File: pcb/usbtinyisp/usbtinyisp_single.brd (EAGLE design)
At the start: 44 x 36 mm, 27 parts, among them IC1 ATTINY2313-20P, IC2 74LVX125D, Q1 12000

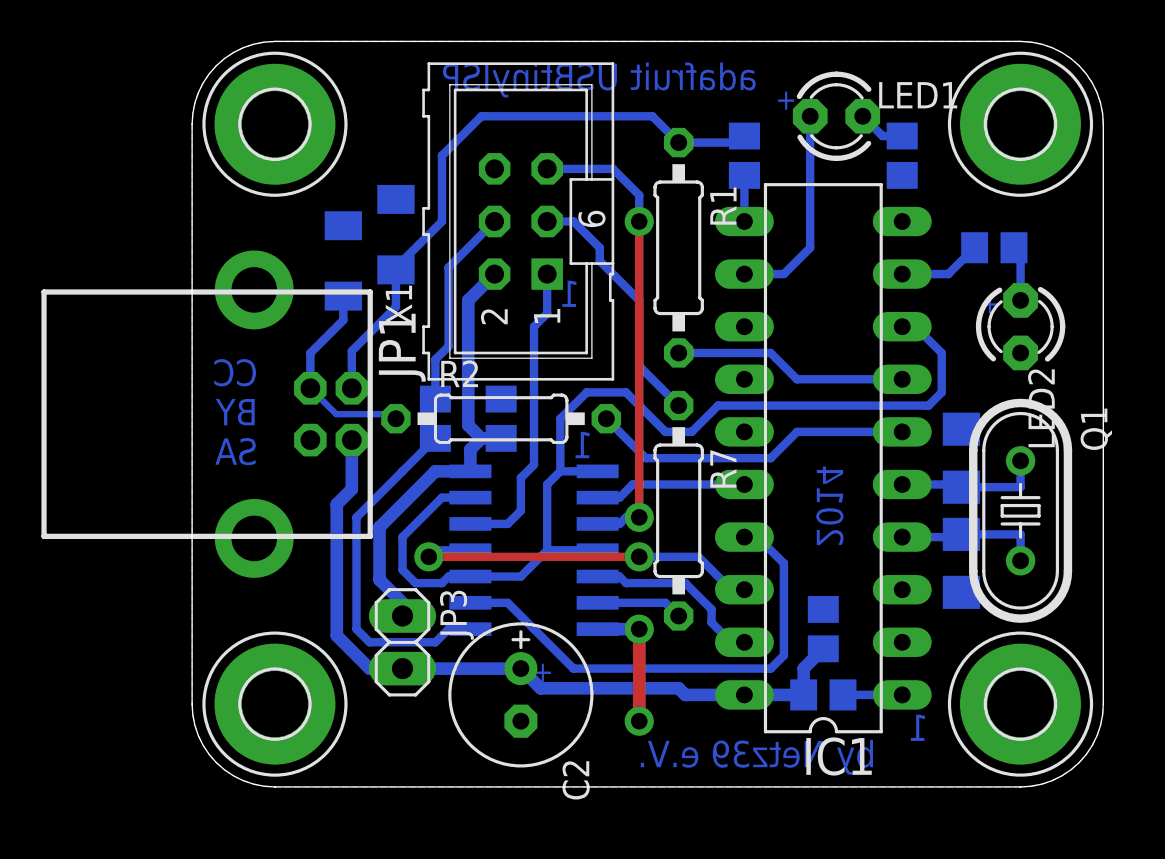
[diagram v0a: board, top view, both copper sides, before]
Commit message: swap LED1 with resistor
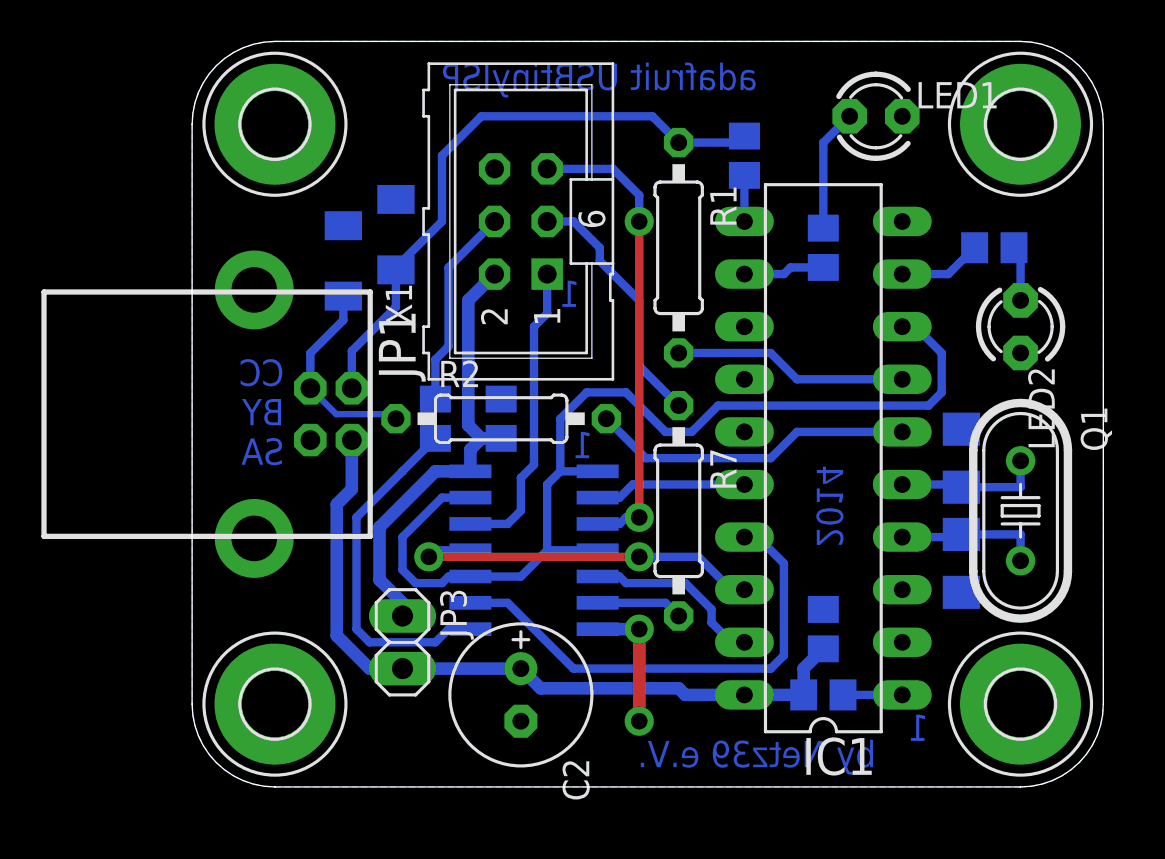
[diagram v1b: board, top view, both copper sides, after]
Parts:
- moved R6 5.85 mm to (30.5, 26.0), turned to 270 degrees
- moved LED1 1.91 mm to (33.0, 32.4)
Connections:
- removed net N$8: LED1.K, R6.2
- new net N$5: LED1.A, R6.1
- net GND: now also LED1.K; no longer R6.1
- net N$7: now also R6.2; no longer LED1.A
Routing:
- net N$7: track 10.1 -> 3.94 mm
- net N$5: track 0.00 -> 5.93 mm
- net N$8: track 2.30 -> 0.00 mm
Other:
- board text removed: "+"
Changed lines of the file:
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@@
 <setting verticaltext="up"/>
 </settings>
-<grid distance="25" unitdist="mil" unit="mil" style="dots" multiple="1" display="yes" altdistance="12.5" altunitdist="mil" altunit="mil"/>
+<grid distance="25" unitdist="mil" unit="mil" style="dots" multiple="1" display="no" altdistance="12.5" altunitdist="mil" altunit="mil"/>
 <layers>
 <layer number="1" name="Top" color="4" fill="1" visible="yes" active="yes"/>
@@
 <text x="27.305" y="33.655" size="1.27" layer="16" font="vector" ratio="15" rot="MR0">adafruit USBtinyISP</text>
 <text x="31.4325" y="15.5575" size="1.27" layer="16" font="vector" ratio="15" rot="MR270">2014</text>
-<text x="3.175" y="15.5575" size="1.27" layer="16" font="vector" ratio="15" rot="MR0">CC
+<text x="4.445" y="15.5575" size="1.27" layer="16" font="vector" ratio="15" rot="MR0">CC
 BY
 SA</text>
@@
 <text x="35.56" y="2.2225" size="1.27" layer="16" font="vector" ratio="13" rot="MR0">1</text>
 <text x="18.7325" y="23.1775" size="1.27" layer="16" font="vector" ratio="13" rot="MR0">1</text>
-<text x="17.4625" y="5.08" size="1.016" layer="16" font="vector" ratio="13" rot="MR0">+</text>
-<text x="39.0525" y="22.86" size="1.016" layer="16" font="vector" ratio="13" rot="MR0">+</text>
-<text x="29.21" y="32.7025" size="1.016" layer="16" font="vector" ratio="13" rot="MR0">+</text>
 </plain>
 <attributes>
@@
 <element name="JP3" library="pinhead" package="1X02" value="PWR" x="10.16" y="6.985" rot="R270"/>
 <element name="C1" library="rcl" package="C0805" value="100n" x="30.48" y="7.62" rot="MR90"/>
-<element name="LED1" library="minimidi" package="LED3MM" value="" x="31.115" y="32.385"/>
-<element name="R6" library="rcl" package="R0805" value="1k5" x="34.29" y="30.48" rot="MR90"/>
+<element name="LED1" library="minimidi" package="LED3MM" value="" x="33.02" y="32.385"/>
+<element name="R6" library="rcl" package="R0805" value="1k5" x="30.48" y="26.035" rot="MR270"/>
 <element name="D1" library="diode" package="SOD80C" value="3V6" x="7.3025" y="25.4" rot="MR90"/>
 <element name="D2" library="diode" package="SOD80C" value="3V6" x="9.8425" y="26.67" rot="MR90"/>
@@
 <contactref element="D1" pad="A"/>
 <contactref element="LED2" pad="K"/>
-<contactref element="R6" pad="1"/>
 <contactref element="JP1" pad="6"/>
 <contactref element="X1" pad="4"/>
@@
 <wire x1="19.5834" y1="7.62" x2="21.59" y2="7.62" width="0.6096" layer="16"/>
 <contactref element="C5" pad="2"/>
+<contactref element="LED1" pad="K"/>
 </signal>
 <signal name="N$6">
@@
 <wire x1="40.005" y1="23.495" x2="40.005" y2="25.715" width="0.4064" layer="16"/>
 <wire x1="40.005" y1="25.715" x2="39.685" y2="26.035" width="0.4064" layer="16"/>
-</signal>
-<signal name="N$7">
-<contactref element="IC1" pad="12"/>
-<contactref element="LED1" pad="A"/>
-<wire x1="26.67" y1="24.765" x2="28.575" y2="24.765" width="0.4064" layer="16"/>
-<wire x1="28.575" y1="24.765" x2="29.845" y2="26.035" width="0.4064" layer="16"/>
-<wire x1="29.845" y1="26.035" x2="29.845" y2="32.385" width="0.4064" layer="16"/>
-</signal>
-<signal name="N$8">
-<contactref element="R6" pad="2"/>
-<contactref element="LED1" pad="K"/>
-<wire x1="32.385" y1="32.385" x2="33.34" y2="31.43" width="0.4064" layer="16"/>
-<wire x1="33.34" y1="31.43" x2="34.29" y2="31.43" width="0.4064" layer="16"/>
 </signal>
 <signal name="N$12">
@@
 <signal name="N$4">
 </signal>
+<signal name="N$5">
+<contactref element="LED1" pad="A"/>
+<contactref element="R6" pad="1"/>
+<wire x1="31.75" y1="32.385" x2="30.48" y2="31.115" width="0.4064" layer="16"/>
+<wire x1="30.48" y1="31.115" x2="30.48" y2="26.985" width="0.4064" layer="16"/>
+</signal>
+<signal name="N$7">
+<contactref element="R6" pad="2"/>
+<contactref element="IC1" pad="12"/>
+<wire x1="26.67" y1="24.765" x2="28.575" y2="24.765" width="0.4064" layer="16"/>
+<wire x1="30.48" y1="25.085" x2="28.895" y2="25.085" width="0.4064" layer="16"/>
+<wire x1="28.895" y1="25.085" x2="28.575" y2="24.765" width="0.4064" layer="16"/>
+</signal>
 </signals>
